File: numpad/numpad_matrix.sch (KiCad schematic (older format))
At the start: 34 parts, among them SW10 NUM2, SW11 NUM., SW12 NUM*, SW13 NUM9, SW14 NUM6, SW15 NUM3, SW16 NUM-, SW17 NUM+, SW18 NUM_ENTER, SW2 NUMLOCK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

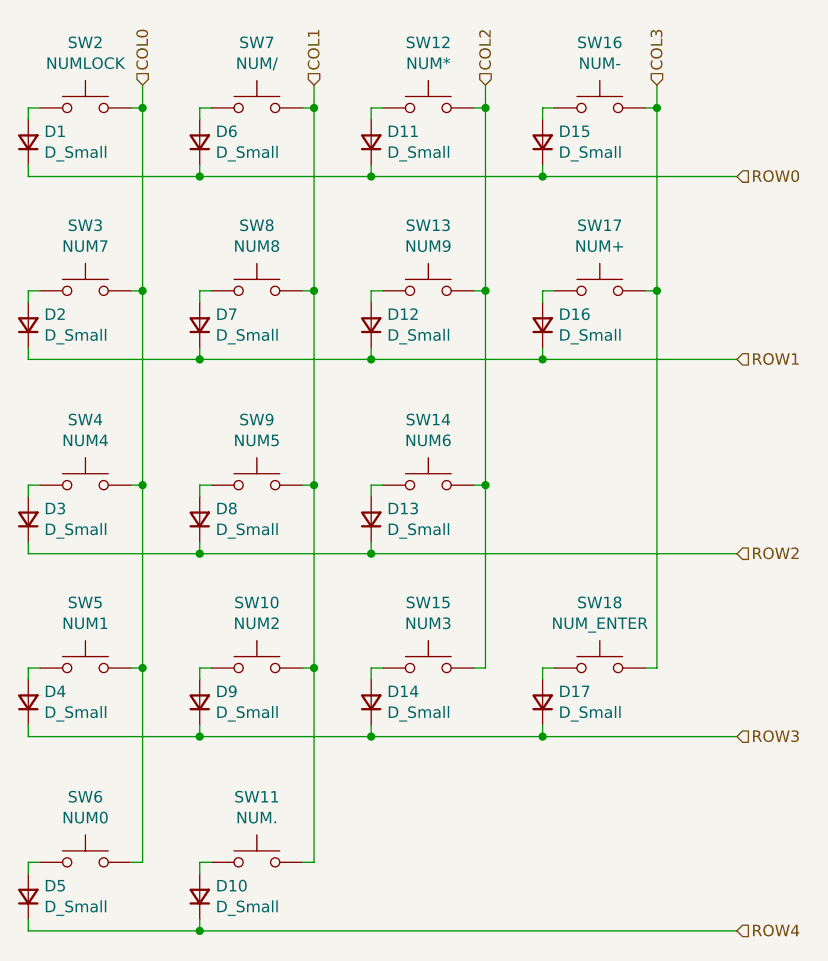
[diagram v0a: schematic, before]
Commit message: Route the rest of numpad
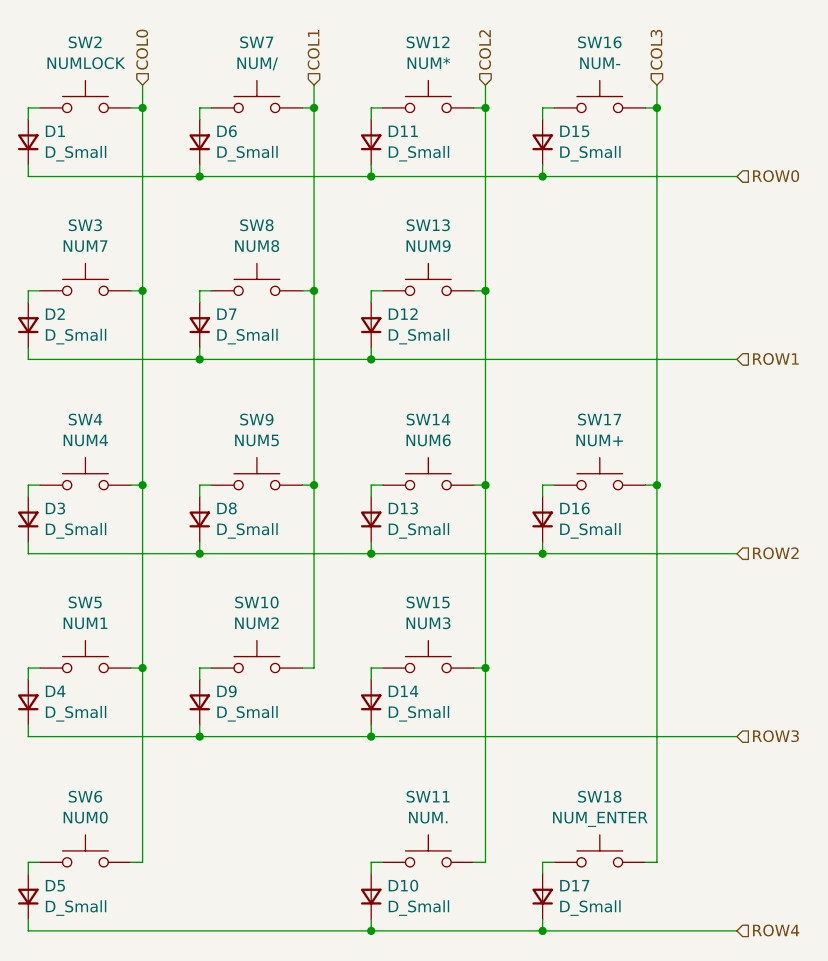
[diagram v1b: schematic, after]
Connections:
- net COL1: no longer SW11.2
- net COL2: now also SW11.2
- net ROW1: no longer D16.1 (K)
- net ROW2: now also D16.1 (K)
- net ROW3: no longer D17.1 (K)
- net ROW4: now also D17.1 (K)
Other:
- moved on the sheet: D10, D16, D17, SW11, SW17, SW18
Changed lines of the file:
@@
 L Switch:SW_Push SW?
 U 1 1 5F46906F
-P 3400 2000
+P 3400 2850
 AR Path="/5F46906F" Ref="SW?"  Part="1"
 AR Path="/5F401E16/5F46906F" Ref="SW?"  Part="1"
 AR Path="/5F428B3F/5F46906F" Ref="SW17"  Part="1"
-F 0 "SW17" H 3400 2285 50  0000 C CNN
-F 1 "NUM+" H 3400 2194 50  0000 C CNN
-F 2 "Button_Switch_Keyboard_MX_Alps_Hybrid:MX-2U" H 3400 2200 50  0001 C CNN
-F 3 "~" H 3400 2200 50  0001 C CNN
-	1    3400 2000
+F 0 "SW17" H 3400 3135 50  0000 C CNN
+F 1 "NUM+" H 3400 3044 50  0000 C CNN
+F 2 "Button_Switch_Keyboard_MX_Alps_Hybrid:MX-2U" H 3400 3050 50  0001 C CNN
+F 3 "~" H 3400 3050 50  0001 C CNN
+	1    3400 2850
 	1    0    0    -1
 $EndComp
@@
 L Device:D_Small D16
 U 1 1 5F469075
-P 3150 2150
-F 0 "D16" V 3196 2080 50  0000 R CNN
-F 1 "D_Small" V 3105 2080 50  0000 R CNN
-F 2 "Diode_SMD:D_SOD-123F" V 3150 2150 50  0001 C CNN
-F 3 "~" V 3150 2150 50  0001 C CNN
-	1    3150 2150
-	0    -1   -1   0
-$EndComp
-Wire Wire Line
-	3200 2000 3150 2000
-Wire Wire Line
-	3150 2000 3150 2050
-Wire Wire Line
-	3150 2300 3150 2250
-Wire Wire Line
-	3600 2000 3650 2000
+P 3150 3000
+F 0 "D16" V 3196 2930 50  0000 R CNN
+F 1 "D_Small" V 3105 2930 50  0000 R CNN
+F 2 "Diode_SMD:D_SOD-123F" V 3150 3000 50  0001 C CNN
+F 3 "~" V 3150 3000 50  0001 C CNN
+	1    3150 3000
+	0    -1   -1   0
+$EndComp
+Wire Wire Line
+	3200 2850 3150 2850
+Wire Wire Line
+	3150 2850 3150 2900
+Wire Wire Line
+	3150 3150 3150 3100
+Wire Wire Line
+	3600 2850 3650 2850
 $Comp
 L Switch:SW_Push SW4
@@
 L Switch:SW_Push SW?
 U 1 1 5F46923F
-P 3400 3650
+P 3400 4500
 AR Path="/5F46923F" Ref="SW?"  Part="1"
 AR Path="/5F401E16/5F46923F" Ref="SW?"  Part="1"
 AR Path="/5F428B3F/5F46923F" Ref="SW18"  Part="1"
-F 0 "SW18" H 3400 3935 50  0000 C CNN
-F 1 "NUM_ENTER" H 3400 3844 50  0000 C CNN
-F 2 "Button_Switch_Keyboard_MX_Alps_Hybrid:MX-2U" H 3400 3850 50  0001 C CNN
-F 3 "~" H 3400 3850 50  0001 C CNN
-	1    3400 3650
+F 0 "SW18" H 3400 4785 50  0000 C CNN
+F 1 "NUM_ENTER" H 3400 4694 50  0000 C CNN
+F 2 "Button_Switch_Keyboard_MX_Alps_Hybrid:MX-2U" H 3400 4700 50  0001 C CNN
+F 3 "~" H 3400 4700 50  0001 C CNN
+	1    3400 4500
 	1    0    0    -1
 $EndComp
@@
 L Device:D_Small D17
 U 1 1 5F469245
-P 3150 3800
-F 0 "D17" V 3196 3730 50  0000 R CNN
-F 1 "D_Small" V 3105 3730 50  0000 R CNN
-F 2 "Diode_SMD:D_SOD-123F" V 3150 3800 50  0001 C CNN
-F 3 "~" V 3150 3800 50  0001 C CNN
-	1    3150 3800
-	0    -1   -1   0
-$EndComp
-Wire Wire Line
-	3200 3650 3150 3650
-Wire Wire Line
-	3150 3650 3150 3700
-Wire Wire Line
-	3150 3950 3150 3900
-Wire Wire Line
-	3600 3650 3650 3650
+P 3150 4650
+F 0 "D17" V 3196 4580 50  0000 R CNN
+F 1 "D_Small" V 3105 4580 50  0000 R CNN
+F 2 "Diode_SMD:D_SOD-123F" V 3150 4650 50  0001 C CNN
+F 3 "~" V 3150 4650 50  0001 C CNN
+	1    3150 4650
+	0    -1   -1   0
+$EndComp
+Wire Wire Line
+	3200 4500 3150 4500
+Wire Wire Line
+	3150 4500 3150 4550
+Wire Wire Line
+	3150 4800 3150 4750
+Wire Wire Line
+	3600 4500 3650 4500
 $Comp
 L Switch:SW_Push SW?
@@
 	1350 4500 1400 4500
 $Comp
-L Switch:SW_Push SW?
-U 1 1 5F4692FF
-P 1900 4500
-AR Path="/5F4692FF" Ref="SW?"  Part="1"
-AR Path="/5F401E16/5F4692FF" Ref="SW?"  Part="1"
-AR Path="/5F428B3F/5F4692FF" Ref="SW11"  Part="1"
-F 0 "SW11" H 1900 4785 50  0000 C CNN
-F 1 "NUM." H 1900 4694 50  0000 C CNN
-F 2 "Button_Switch_Keyboard_MX_Alps_Hybrid:MX-1U" H 1900 4700 50  0001 C CNN
-F 3 "~" H 1900 4700 50  0001 C CNN
-	1    1900 4500
-	1    0    0    -1
-$EndComp
-$Comp
 L Device:D_Small D10
 U 1 1 5F469305
-P 1650 4650
-F 0 "D10" V 1696 4580 50  0000 R CNN
-F 1 "D_Small" V 1605 4580 50  0000 R CNN
-F 2 "Diode_SMD:D_SOD-123F" V 1650 4650 50  0001 C CNN
-F 3 "~" V 1650 4650 50  0001 C CNN
-	1    1650 4650
-	0    -1   -1   0
-$EndComp
-Wire Wire Line
-	1700 4500 1650 4500
-Wire Wire Line
-	1650 4500 1650 4550
-Wire Wire Line
-	1650 4800 1650 4750
-Wire Wire Line
-	2100 4500 2150 4500
+P 2400 4650
+F 0 "D10" V 2446 4580 50  0000 R CNN
+F 1 "D_Small" V 2355 4580 50  0000 R CNN
+F 2 "Diode_SMD:D_SOD-123F" V 2400 4650 50  0001 C CNN
+F 3 "~" V 2400 4650 50  0001 C CNN
+	1    2400 4650
+	0    -1   -1   0
+$EndComp
+Wire Wire Line
+	2450 4500 2400 4500
+Wire Wire Line
+	2400 4500 2400 4550
 Wire Wire Line
 	1400 1200 1400 2000
@@
 Wire Wire Line
 	2150 2850 2150 2000
-Connection ~ 2150 3650
 Wire Wire Line
 	2150 3650 2150 2850
-Wire Wire Line
-	2150 4500 2150 3650
 Wire Wire Line
 	2900 1200 2900 2000
@@
 	2900 2850 2900 3650
 Wire Wire Line
-	3650 1200 3650 2000
-Connection ~ 3650 2000
-Wire Wire Line
 	1650 1500 2400 1500
 Connection ~ 2400 1500
@@
 Connection ~ 2400 2300
 Wire Wire Line
-	2400 2300 3150 2300
-Wire Wire Line
 	900  3150 1650 3150
 Connection ~ 1650 3150
@@
 	1650 3950 2400 3950
 Connection ~ 2400 3950
-Wire Wire Line
-	2400 3950 3150 3950
-Connection ~ 3150 3950
-Wire Wire Line
-	900  4800 1650 4800
-Connection ~ 1650 4800
 Wire Wire Line
 	1400 1200 1400 1100
@@
 Connection ~ 1650 1500
 Wire Wire Line
-	4000 2300 3150 2300
-Connection ~ 3150 2300
-Wire Wire Line
-	3650 2000 3650 3650
-Wire Wire Line
-	3150 3950 4000 3950
-Wire Wire Line
-	4000 3150 2400 3150
+	4000 3150 3150 3150
 Connection ~ 2400 3150
-Wire Wire Line
-	1650 4800 4000 4800
 $Comp
 L Switch:SW_Push SW?
@@
 	1    0    0    -1
 $EndComp
+Wire Wire Line
+	2900 4500 2900 3650
+Wire Wire Line
+	2850 4500 2900 4500
+$Comp
+L Switch:SW_Push SW?
+U 1 1 5F4692FF
+P 2650 4500
+AR Path="/5F4692FF" Ref="SW?"  Part="1"
+AR Path="/5F401E16/5F4692FF" Ref="SW?"  Part="1"
+AR Path="/5F428B3F/5F4692FF" Ref="SW11"  Part="1"
+F 0 "SW11" H 2650 4785 50  0000 C CNN
+F 1 "NUM." H 2650 4694 50  0000 C CNN
+F 2 "Button_Switch_Keyboard_MX_Alps_Hybrid:MX-1U" H 2650 4700 50  0001 C CNN
+F 3 "~" H 2650 4700 50  0001 C CNN
+	1    2650 4500
+	1    0    0    -1
+$EndComp
+Connection ~ 2900 3650
+Wire Wire Line
+	2400 4750 2400 4800
+Connection ~ 2400 4800
+Wire Wire Line
+	2400 4800 3150 4800
+Wire Wire Line
+	900  4800 2400 4800
+Connection ~ 3150 3150
+Wire Wire Line
+	3150 3150 2400 3150
+Connection ~ 3650 2850
+Wire Wire Line
+	3650 1200 3650 2850
+Wire Wire Line
+	2400 2300 4000 2300
+Connection ~ 3150 4800
+Wire Wire Line
+	3150 4800 4000 4800
+Wire Wire Line
+	2400 3950 4000 3950
+Wire Wire Line
+	3650 2850 3650 4500
 $EndSCHEMATC
